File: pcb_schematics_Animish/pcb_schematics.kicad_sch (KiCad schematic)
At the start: 73 parts, among them J1 CUE_SJ1-352XNG, J2 Conn_01x01_Pin, J3 Conn_01x05, J4 Conn_01x05, J5 Conn_01x05, SW1 SW_Push, U2 RDA5807M_Module, U3 LM386, U4 LM386, U5 RPi_Pico_TH

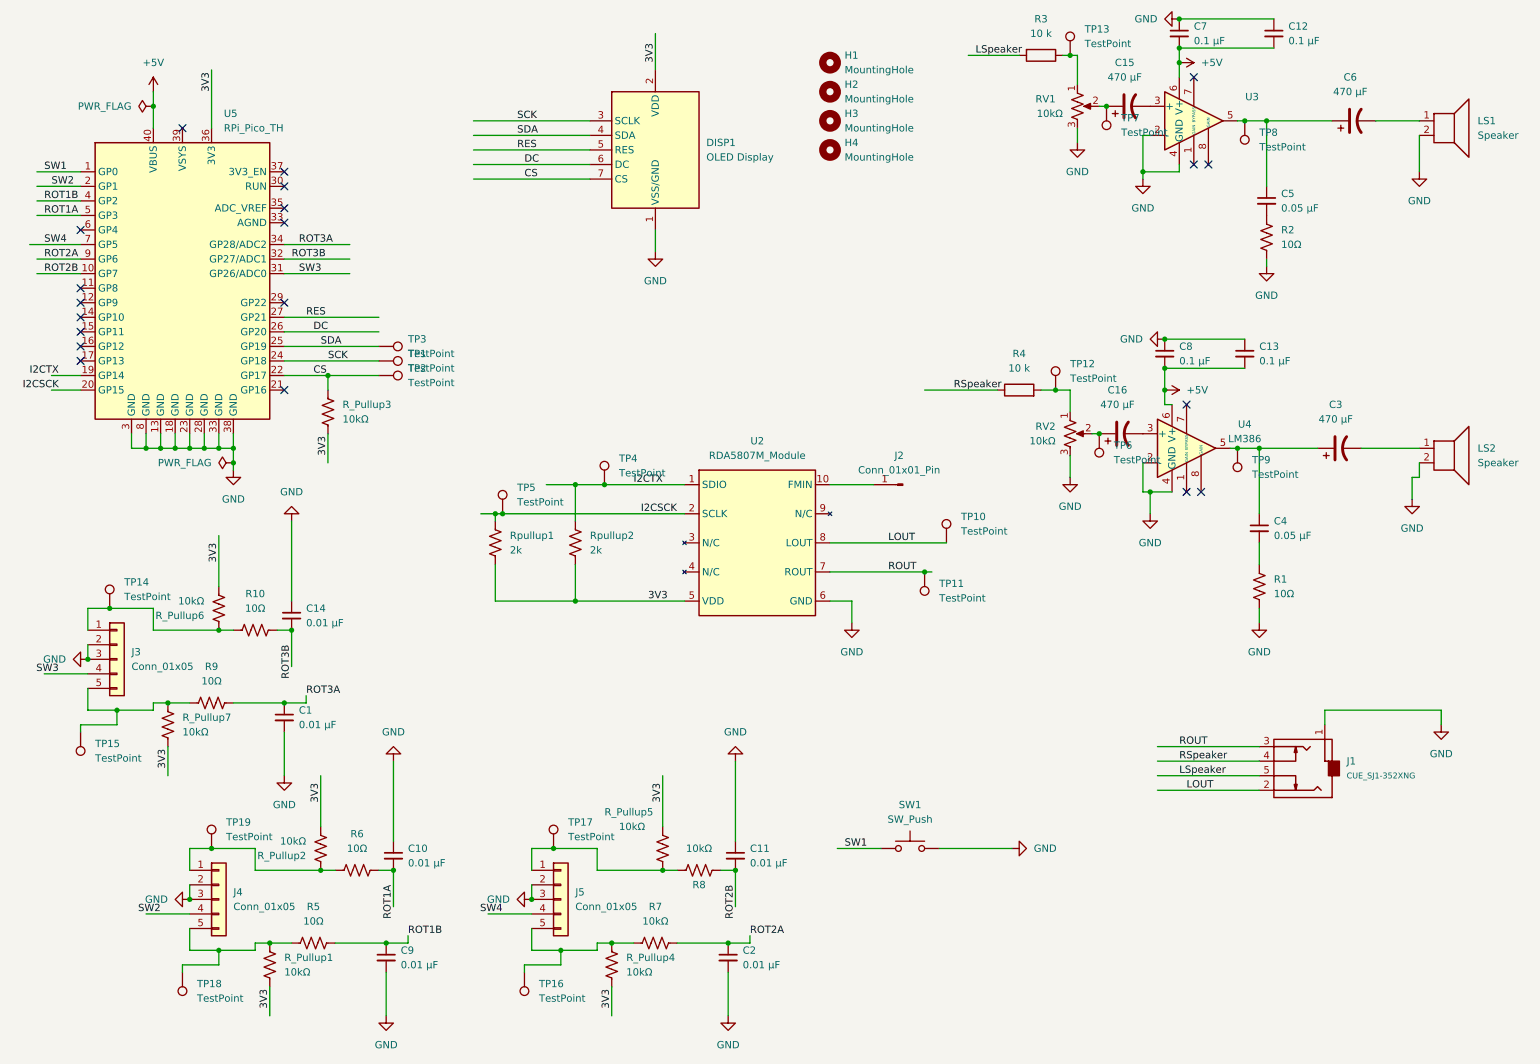
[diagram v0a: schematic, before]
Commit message: modified the webpage and set up the main files
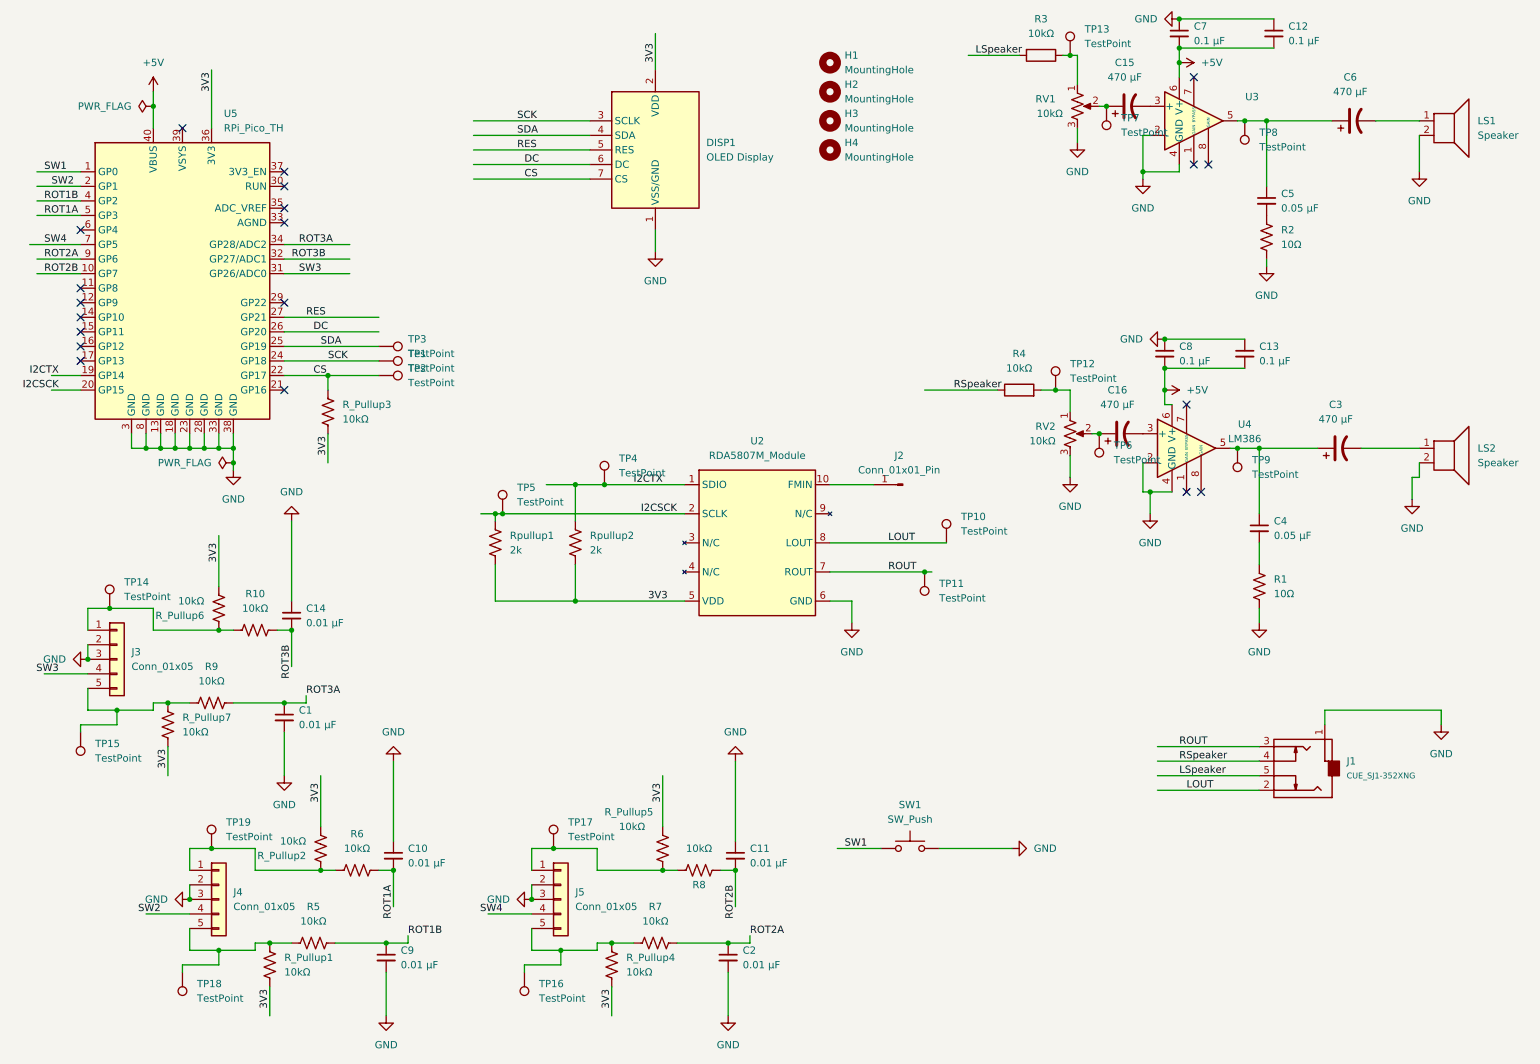
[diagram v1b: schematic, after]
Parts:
- R10, R5, R6, R9: value 10Ω -> 10kΩ
- R3, R4: value 10 k -> 10kΩ
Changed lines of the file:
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@@
 			)
 		)
-		(property "Value" "10Ω"
+		(property "Value" "10kΩ"
 			(at 58.42 116.84 90)
 			(effects
@@
 			)
 		)
-		(property "Value" "10Ω"
+		(property "Value" "10kΩ"
 			(at 68.58 171.45 90)
 			(effects
@@
 			)
 		)
-		(property "Value" "10Ω"
+		(property "Value" "10kΩ"
 			(at 76.2 158.75 90)
 			(effects
@@
 			)
 		)
-		(property "Value" "10 k"
+		(property "Value" "10kΩ"
 			(at 191.77 74.93 90)
 			(effects
@@
 			)
 		)
-		(property "Value" "10 k"
+		(property "Value" "10kΩ"
 			(at 195.58 16.51 90)
 			(effects
@@
 			)
 		)
-		(property "Value" "10Ω"
+		(property "Value" "10kΩ"
 			(at 50.8 129.54 90)
 			(effects
